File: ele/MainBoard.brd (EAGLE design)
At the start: 136.6 x 100 mm, 116 parts, among them IC1 MCP23017SP, IC2 74HC595D, IC3 74HC595D, X1 POWER_IN, X2 POWER_OUT

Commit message: ele: Finish routing v1.1
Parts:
- moved JP20 167.3 mm to (61.6, 93.3), turned to 90 degrees
- moved R18 126.8 mm to (55.9, 67.3)
- moved Q4 97.0 mm to (55.9, 71.8), turned to 180 degrees
- moved Q1 9.52 mm to (51.4, 14.0), turned to 0 degrees
- moved TP4 6.63 mm to (49.5, 90.2)
- moved JP24 5.08 mm to (58.4, 93.3)
- moved JP11 4.45 mm to (55.2, 93.3)
- moved TP3 4.26 mm to (49.5, 98.4)
- moved R8 3.86 mm to (55.9, 84.5), turned to 90 degrees
- moved Q2 3.86 mm to (55.9, 61.6), turned to 180 degrees
- moved JP21 3.81 mm to (52.1, 93.3)
- moved D1 3.59 mm to (57.1, 64.8)
- moved JP14 3.18 mm to (50.2, 26.0)
- moved JP17 3.18 mm to (55.2, 26.0)
- moved IM1 2.62 mm to (52.7, 50.8)
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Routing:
- net N$1: track 0.00 -> 92.7 mm, vias 0 -> 1
- net BAT_PROT: track 6.35 -> 89.9 mm, vias 0 -> 1
- net EN: track 228.1 -> 265.8 mm
- net N$6: track 0.00 -> 30.3 mm
- net +3V3: track 512.9 -> 542.5 mm, vias 18 -> 20
- net ESP_!SHUTDOWN: track 77.3 -> 101.4 mm, vias 1 -> 2
- net VCC: track 17.1 -> 28.6 mm, vias 0 -> 1
- net BAT: track 6.72 -> 0.00 mm
- net RCKMOT: track 216.6 -> 211.5 mm
- net +5V: track 208.9 -> 204.7 mm
- net ENC8A: track 140.8 -> 136.8 mm
- net _EN_: track 0.00 -> 3.44 mm
- net ENC1A: track 154.0 -> 151.5 mm
- net SCL: track 345.0 -> 342.4 mm
- net ENC6B: track 135.4 -> 132.9 mm
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- added copper zone on layer 16, net BAT
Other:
- board size 136.6 x 100 mm -> 134.1 x 100 mm
- board text added: "+5V"
- board text added: "ESP !SHDN"
- board text removed: "ESP !SHUTDOWN"

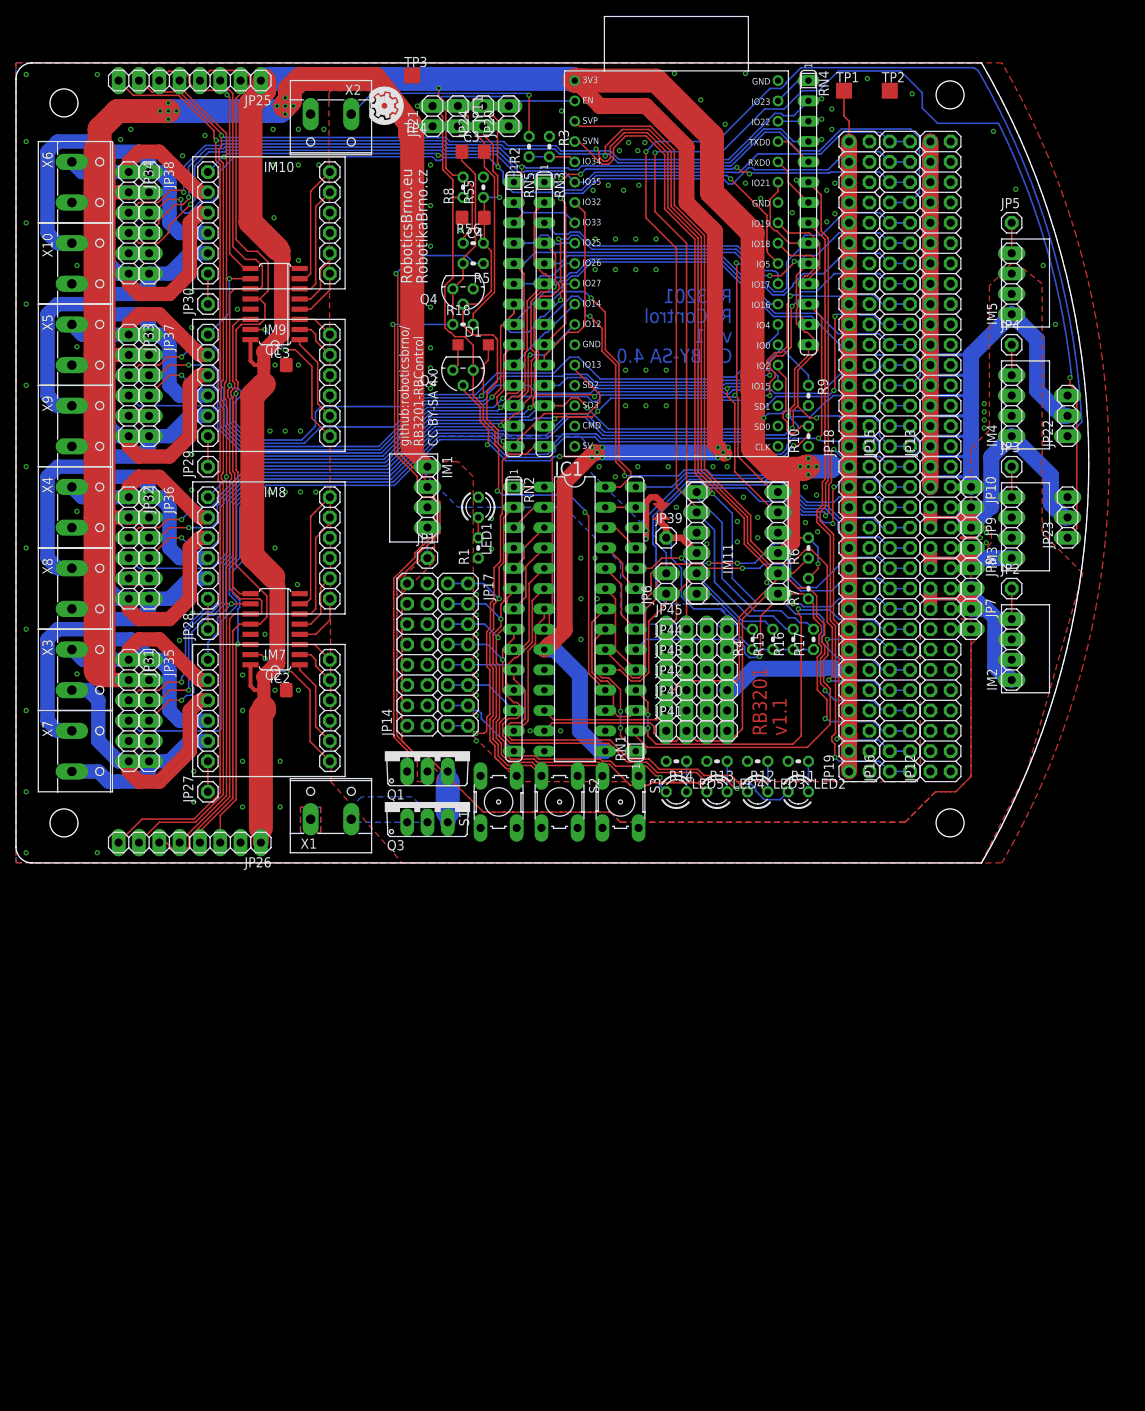
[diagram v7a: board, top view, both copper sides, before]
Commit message: ele: Round two remaining corners
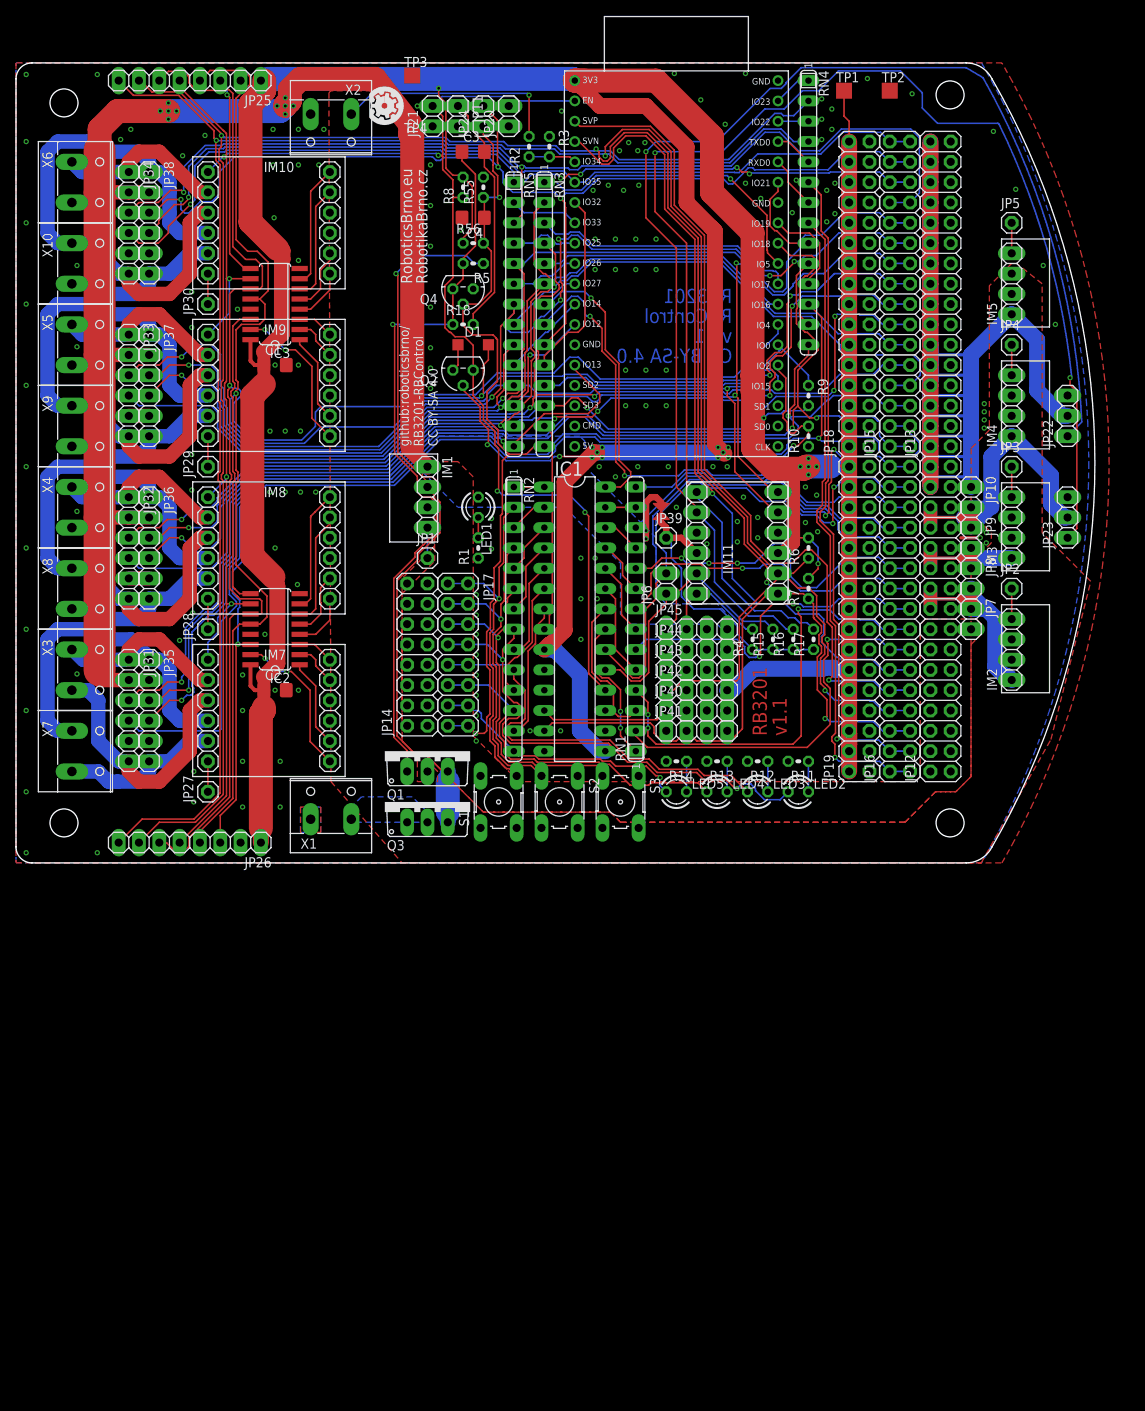
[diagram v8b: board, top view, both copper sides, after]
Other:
- board size 134.1 x 100 mm -> 134.9 x 100 mm
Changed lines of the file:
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@@
 <setting verticaltext="up"/>
 </settings>
-<grid distance="0.025" unitdist="inch" unit="mil" style="lines" multiple="1" display="yes" altdistance="0.01" altunitdist="inch" altunit="mil"/>
+<grid distance="1" unitdist="mm" unit="mm" style="lines" multiple="1" display="yes" altdistance="0.1" altunitdist="mm" altunit="mm"/>
 <layers>
 <layer number="1" name="Top" color="4" fill="1" visible="yes" active="yes"/>
@@
 <board>
 <plain>
-<wire x1="120.7" y1="0" x2="120.7" y2="100" width="0" layer="20" curve="60"/>
-<wire x1="120.7" y1="100" x2="2" y2="100" width="0" layer="20"/>
+<wire x1="122" y1="2" x2="122" y2="98" width="0" layer="20" curve="60"/>
+<wire x1="122" y1="98" x2="118.763934375" y2="100" width="0" layer="20" curve="63.434927"/>
+<wire x1="118.763934375" y1="100" x2="2" y2="100" width="0" layer="20"/>
 <wire x1="2" y1="100" x2="0" y2="98" width="0" layer="20" curve="90"/>
 <wire x1="0" y1="98" x2="0" y2="2" width="0" layer="20"/>
 <wire x1="0" y1="2" x2="2" y2="0" width="0" layer="20" curve="90"/>
-<wire x1="2" y1="0" x2="120.7" y2="0" width="0" layer="20"/>
+<wire x1="2" y1="0" x2="118.763934375" y2="0" width="0" layer="20"/>
+<wire x1="118.763934375" y1="0" x2="122" y2="2" width="0" layer="20" curve="63.434971"/>
 <hole x="6" y="5" drill="3.5"/>
 <hole x="6" y="95" drill="3.5"/>
@@
 <vertex x="48.26" y="0"/>
 <vertex x="120.65" y="0"/>
-<vertex x="126.365" y="11.43"/>
-<vertex x="133.35" y="36.195"/>
+<vertex x="129.365" y="15.43"/>
+<vertex x="134.35" y="35.195"/>
 <vertex x="128.27" y="41.275"/>
 <vertex x="128.27" y="72.39"/>
@@
 <wire x1="132.687796875" y1="54.582796875" x2="131.445" y2="53.34" width="0.2" layer="16"/>
 <wire x1="131.445" y1="53.34" x2="133.219515625" y2="55.114515625" width="0.2" layer="16"/>
-<wire x1="133.219515625" y1="55.114515625" x2="120.269" y2="99.06" width="0.2" layer="16" curve="27"/>
-<wire x1="120.269" y1="99.06" x2="119.675" y2="99.4" width="0.2" layer="16"/>
-<wire x1="119.675" y1="99.4" x2="98.13" y2="99.4" width="0.2" layer="16"/>
+<wire x1="133.219515625" y1="55.114515625" x2="120.869" y2="98.16" width="0.2" layer="16" curve="27"/>
+<wire x1="120.869" y1="98.16" x2="118.775" y2="99.4" width="0.2" layer="16"/>
+<wire x1="118.775" y1="99.4" x2="98.13" y2="99.4" width="0.2" layer="16"/>
 <wire x1="85.09" y1="43.815" x2="85.09" y2="44.45" width="0.2" layer="1"/>
 <wire x1="85.09" y1="44.45" x2="82.55" y2="46.99" width="0.2" layer="1"/>
